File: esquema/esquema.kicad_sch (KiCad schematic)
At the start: 16 parts

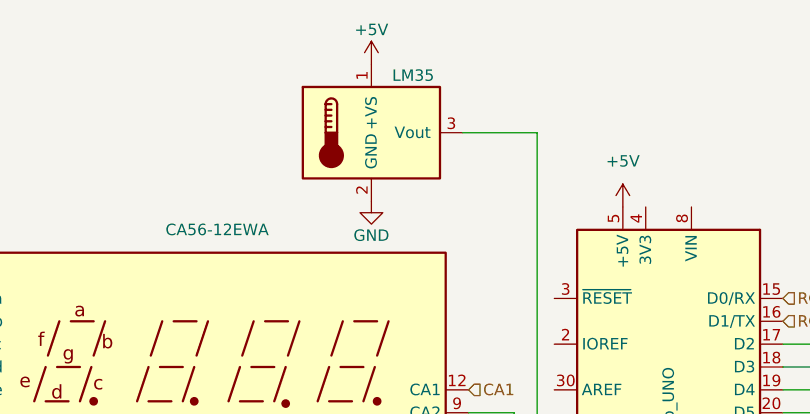
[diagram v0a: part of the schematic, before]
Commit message: Include temperature reading
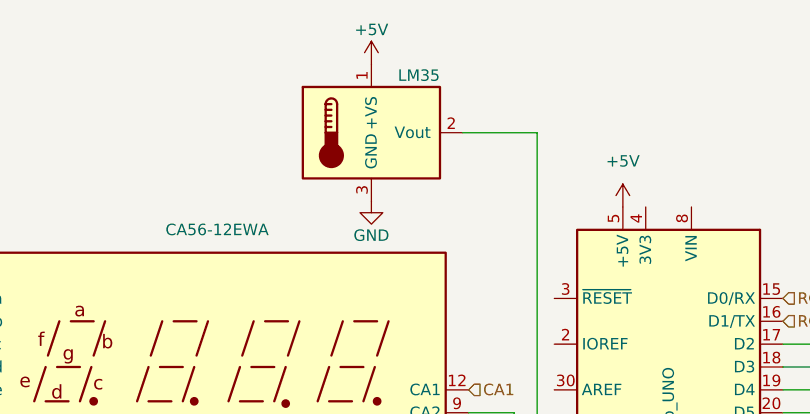
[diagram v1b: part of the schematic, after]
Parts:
- removed U?: LM35, symbol Sensor_Temperature:LM35-NEB
- added U?: LM35, symbol Sensor_Temperature:LM35-LP
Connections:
- net +5V: now also U?.1 (+VS)
- net GND: now also U?.3 (GND)
- net at A?.9 (A0): now also U?.2 (Vout)
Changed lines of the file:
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@@
     (pin "1")
-  )
-  (symbol (lib_id "Sensor_Temperature:LM35-NEB") (at 116.205 52.705 0) (unit 1)
-    (in_bom yes) (on_board yes)
-    (property "Reference" "U?" (id 0) (at 106.68 51.4349 0)
-      (effects (font (size 1.27 1.27)) (justify right) hide)
-    )
-    (property "Value" "LM35" (id 1) (at 123.19 46.355 0)
-      (effects (font (size 1.27 1.27)) (justify right))
-    )
-    (property "Footprint" "" (id 2) (at 117.475 59.055 0)
-      (effects (font (size 1.27 1.27)) (justify left) hide)
-    )
-    (property "Datasheet" "http://www.ti.com/lit/ds/symlink/lm35.pdf" (id 3) (at 116.205 52.705 0)
-      (effects (font (size 1.27 1.27)) hide)
-    )
-    (pin "1")
-    (pin "2")
-    (pin "3")
   )
   (symbol (lib_id "Memory_EEPROM:AT24CS16-SSHM") (at 141.605 129.54 0) (mirror y) (unit 1)
@@
     (pin "1")
   )
+  (symbol (lib_id "Sensor_Temperature:LM35-LP") (at 116.205 52.705 0) (unit 1)
+    (in_bom yes) (on_board yes)
+    (property "Reference" "U?" (id 0) (at 107.315 51.4349 0)
+      (effects (font (size 1.27 1.27)) (justify right) hide)
+    )
+    (property "Value" "LM35" (id 1) (at 123.825 46.355 0)
+      (effects (font (size 1.27 1.27)) (justify right))
+    )
+    (property "Footprint" "" (id 2) (at 117.475 59.055 0)
+      (effects (font (size 1.27 1.27)) (justify left) hide)
+    )
+    (property "Datasheet" "http://www.ti.com/lit/ds/symlink/lm35.pdf" (id 3) (at 116.205 52.705 0)
+      (effects (font (size 1.27 1.27)) hide)
+    )
+    (pin "1")
+    (pin "2")
+    (pin "3")
+  )
   (symbol (lib_id "power:GND") (at 141.605 137.16 0) (unit 1)
     (in_bom yes) (on_board yes) (fields_autoplaced)
@@
       (reference "U?") (unit 1) (value "PCF8574") (footprint "")
     )
-    (path "/64481622-026a-4d73-b295-d39fefb14e90"
-      (reference "U?") (unit 1) (value "LM35") (footprint "")
-    )
     (path "/67672e82-97e4-47ab-b957-cf9ca30dd2f4"
       (reference "U?") (unit 1) (value "AT24CS16-SSHM") (footprint "Package_SO:SOIC-8_3.9x4.9mm_P1.27mm")
@@
       (reference "U?") (unit 1) (value "CA56-12EWA") (footprint "Display_7Segment:CA56-12EWA")
     )
-  )
+    (path "/eebb738b-731b-4116-9d82-911722ba4406"
+      (reference "U?") (unit 1) (value "LM35") (footprint "")
+    )
+  )
